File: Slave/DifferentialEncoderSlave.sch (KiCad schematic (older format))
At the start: 18 parts, among them J1 RJ45_Shielded, U1 SN75C1167, U2 MA730, U3 LDFM33PVR

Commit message: Minor change to encoder transceiver
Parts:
- U1: symbol Wetmelon:SN75C1167 -> DifferentialEncoderSlave-rescue:SN75C1167-Wetmelon
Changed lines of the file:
@@
 $EndDescr
 $Comp
-L Wetmelon:SN75C1167 U1
+L DifferentialEncoderSlave-rescue:SN75C1167-Wetmelon U1
 U 1 1 5F8ED6E6
 P 5750 2650

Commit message: Update Slave
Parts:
- removed C?: 10nF, symbol Device:C_Small
- C1: value 10nF -> 1uF; footprint (none) -> Capacitor_SMD:C_0805_2012Metric
- C2: value 100nF -> 4.7uF; footprint (none) -> Capacitor_SMD:C_0805_2012Metric
- C3, C4, C5, C6: renamed from C?; footprint (none) -> Capacitor_SMD:C_0603_1608Metric
- J1: footprint (none) -> Connector_RJ:RJ45_Amphenol_RJHSE5380
- R1, R2: footprint (none) -> Resistor_SMD:R_0603_1608Metric
- R3, R4, R5, R6, R7: renamed from R?; footprint (none) -> Resistor_SMD:R_0603_1608Metric
- U1: footprint (none) -> Package_SO:TSSOP-16_4.4x5mm_P0.65mm
- U2: footprint Package_DFN_QFN:QFN-16-1EP_3x3mm_P0.5mm_EP1.8x1.8mm -> Package_DFN_QFN:QFN-16-1EP_3x3mm_P0.5mm_EP1.7x1.7mm
- U3: footprint (none) -> Wetmelon:DFN6-2x2; symbol Wetmelon:LDFM33PVR -> DifferentialEncoderSlave-rescue:LDFM33PVR-Wetmelon
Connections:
- wire segments 80 -> 78
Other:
- note added: "Placed close to both\nLDO and MA702"

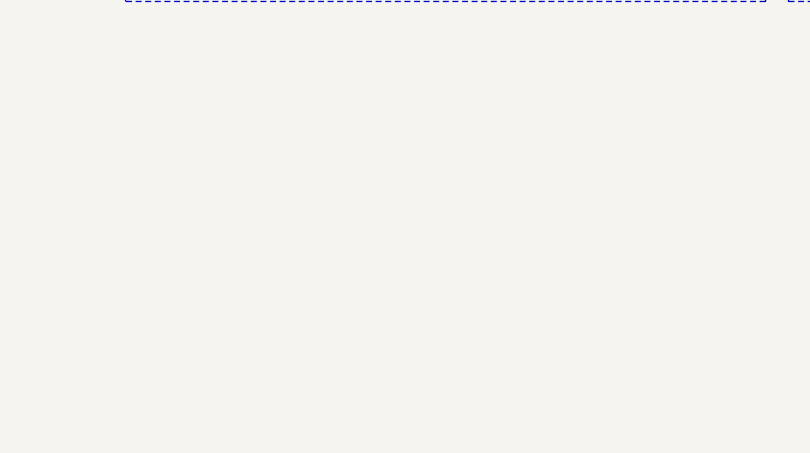
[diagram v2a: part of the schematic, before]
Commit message: Update board outline
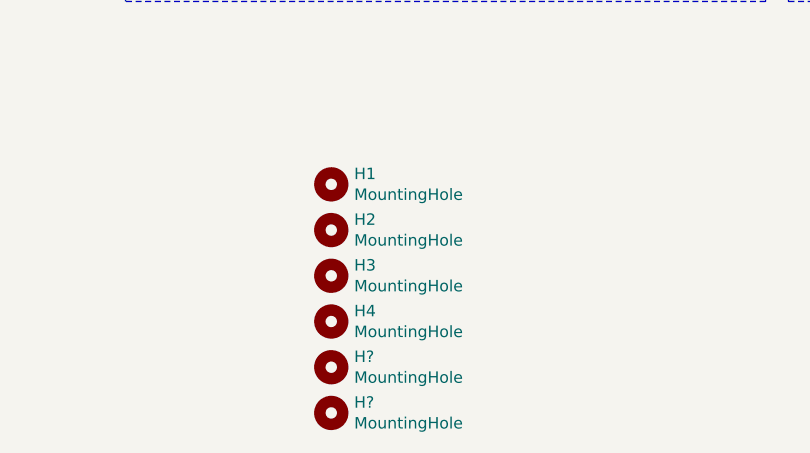
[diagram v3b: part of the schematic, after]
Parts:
- added H1, H2, H3, H4, H? (x2): MountingHole, MountingHole:MountingHole_3.2mm_M3_DIN965, symbol Mechanical:MountingHole
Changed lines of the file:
@@
+	1    0    0    -1
+$EndComp
+$Comp
+L Mechanical:MountingHole H1
+U 1 1 5FCC53CC
+P 5450 6550
+F 0 "H1" H 5550 6596 50  0000 L CNN
+F 1 "MountingHole" H 5550 6505 50  0000 L CNN
+F 2 "MountingHole:MountingHole_3.2mm_M3_DIN965" H 5450 6550 50  0001 C CNN
+F 3 "~" H 5450 6550 50  0001 C CNN
+	1    5450 6550
+	1    0    0    -1
+$EndComp
+$Comp
+L Mechanical:MountingHole H2
+U 1 1 5FCC63AC
+P 5450 6750
+F 0 "H2" H 5550 6796 50  0000 L CNN
+F 1 "MountingHole" H 5550 6705 50  0000 L CNN
+F 2 "MountingHole:MountingHole_3.2mm_M3_DIN965" H 5450 6750 50  0001 C CNN
+F 3 "~" H 5450 6750 50  0001 C CNN
+	1    5450 6750
+	1    0    0    -1
+$EndComp
+$Comp
+L Mechanical:MountingHole H3
+U 1 1 5FCC6701
+P 5450 6950
+F 0 "H3" H 5550 6996 50  0000 L CNN
+F 1 "MountingHole" H 5550 6905 50  0000 L CNN
+F 2 "MountingHole:MountingHole_3.2mm_M3_DIN965" H 5450 6950 50  0001 C CNN
+F 3 "~" H 5450 6950 50  0001 C CNN
+	1    5450 6950
+	1    0    0    -1
+$EndComp
+$Comp
+L Mechanical:MountingHole H4
+U 1 1 5FCC692E
+P 5450 7150
+F 0 "H4" H 5550 7196 50  0000 L CNN
+F 1 "MountingHole" H 5550 7105 50  0000 L CNN
+F 2 "MountingHole:MountingHole_3.2mm_M3_DIN965" H 5450 7150 50  0001 C CNN
+F 3 "~" H 5450 7150 50  0001 C CNN
+	1    5450 7150
+	1    0    0    -1
+$EndComp
+$Comp
+L Mechanical:MountingHole H?
+U 1 1 5FCE01C3
+P 5450 7350
+F 0 "H?" H 5550 7396 50  0000 L CNN
+F 1 "MountingHole" H 5550 7305 50  0000 L CNN
+F 2 "MountingHole:MountingHole_3.2mm_M3_DIN965" H 5450 7350 50  0001 C CNN
+F 3 "~" H 5450 7350 50  0001 C CNN
+	1    5450 7350
+	1    0    0    -1
+$EndComp
+$Comp
+L Mechanical:MountingHole H?
+U 1 1 5FCE01C9
+P 5450 7550
+F 0 "H?" H 5550 7596 50  0000 L CNN
+F 1 "MountingHole" H 5550 7505 50  0000 L CNN
+F 2 "MountingHole:MountingHole_3.2mm_M3_DIN965" H 5450 7550 50  0001 C CNN
+F 3 "~" H 5450 7550 50  0001 C CNN
+	1    5450 7550
 	1    0    0    -1
 $EndComp

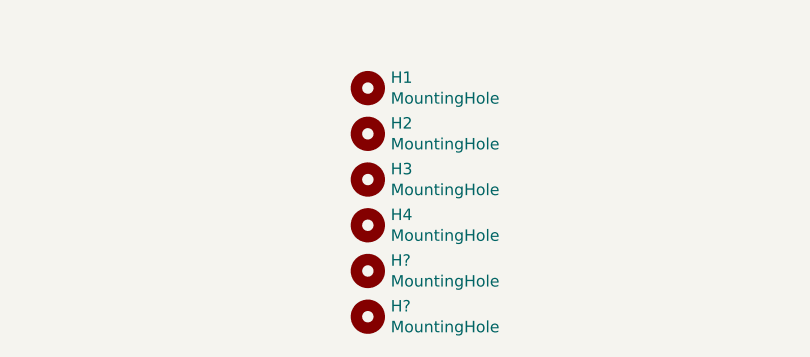
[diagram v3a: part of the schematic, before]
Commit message: Use 3mm holes
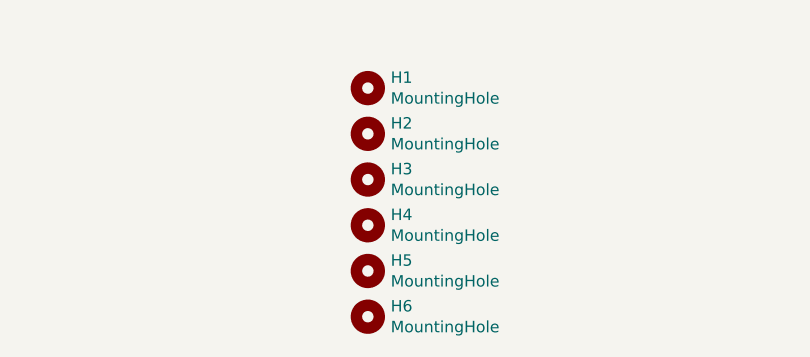
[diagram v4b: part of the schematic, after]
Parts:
- H1, H2, H3, H4: footprint MountingHole:MountingHole_3.2mm_M3_DIN965 -> MountingHole:MountingHole_3mm
- H5, H6: renamed from H?; footprint MountingHole:MountingHole_3.2mm_M3_DIN965 -> MountingHole:MountingHole_3mm
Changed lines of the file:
@@
 F 0 "H1" H 5550 6596 50  0000 L CNN
 F 1 "MountingHole" H 5550 6505 50  0000 L CNN
-F 2 "MountingHole:MountingHole_3.2mm_M3_DIN965" H 5450 6550 50  0001 C CNN
+F 2 "MountingHole:MountingHole_3mm" H 5450 6550 50  0001 C CNN
 F 3 "~" H 5450 6550 50  0001 C CNN
 	1    5450 6550
@@
 F 0 "H2" H 5550 6796 50  0000 L CNN
 F 1 "MountingHole" H 5550 6705 50  0000 L CNN
-F 2 "MountingHole:MountingHole_3.2mm_M3_DIN965" H 5450 6750 50  0001 C CNN
+F 2 "MountingHole:MountingHole_3mm" H 5450 6750 50  0001 C CNN
 F 3 "~" H 5450 6750 50  0001 C CNN
 	1    5450 6750
@@
 F 0 "H3" H 5550 6996 50  0000 L CNN
 F 1 "MountingHole" H 5550 6905 50  0000 L CNN
-F 2 "MountingHole:MountingHole_3.2mm_M3_DIN965" H 5450 6950 50  0001 C CNN
+F 2 "MountingHole:MountingHole_3mm" H 5450 6950 50  0001 C CNN
 F 3 "~" H 5450 6950 50  0001 C CNN
 	1    5450 6950
@@
 F 0 "H4" H 5550 7196 50  0000 L CNN
 F 1 "MountingHole" H 5550 7105 50  0000 L CNN
-F 2 "MountingHole:MountingHole_3.2mm_M3_DIN965" H 5450 7150 50  0001 C CNN
+F 2 "MountingHole:MountingHole_3mm" H 5450 7150 50  0001 C CNN
 F 3 "~" H 5450 7150 50  0001 C CNN
 	1    5450 7150
@@
 $EndComp
 $Comp
-L Mechanical:MountingHole H?
+L Mechanical:MountingHole H5
 U 1 1 5FCE01C3
 P 5450 7350
-F 0 "H?" H 5550 7396 50  0000 L CNN
+F 0 "H5" H 5550 7396 50  0000 L CNN
 F 1 "MountingHole" H 5550 7305 50  0000 L CNN
-F 2 "MountingHole:MountingHole_3.2mm_M3_DIN965" H 5450 7350 50  0001 C CNN
+F 2 "MountingHole:MountingHole_3mm" H 5450 7350 50  0001 C CNN
 F 3 "~" H 5450 7350 50  0001 C CNN
 	1    5450 7350
@@
 $EndComp
 $Comp
-L Mechanical:MountingHole H?
+L Mechanical:MountingHole H6
 U 1 1 5FCE01C9
 P 5450 7550
-F 0 "H?" H 5550 7596 50  0000 L CNN
+F 0 "H6" H 5550 7596 50  0000 L CNN
 F 1 "MountingHole" H 5550 7505 50  0000 L CNN
-F 2 "MountingHole:MountingHole_3.2mm_M3_DIN965" H 5450 7550 50  0001 C CNN
+F 2 "MountingHole:MountingHole_3mm" H 5450 7550 50  0001 C CNN
 F 3 "~" H 5450 7550 50  0001 C CNN
 	1    5450 7550

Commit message: Update Slave with circular keepout, SMD RJ 45
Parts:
- J1: footprint Connector_RJ:RJ45_Amphenol_RJHSE5380 -> Wetmelon:RJLSE4118101
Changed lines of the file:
@@
 F 0 "J1" H 8320 2839 50  0000 R CNN
 F 1 "RJ45_Shielded" H 8320 2748 50  0000 R CNN
-F 2 "Connector_RJ:RJ45_Amphenol_RJHSE5380" V 8650 2825 50  0001 C CNN
+F 2 "Wetmelon:RJLSE4118101" V 8650 2825 50  0001 C CNN
 F 3 "~" V 8650 2825 50  0001 C CNN
 	1    8650 2800

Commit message: Export master BOM
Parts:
- H5, H6: footprint MountingHole:MountingHole_3mm -> MountingHole:MountingHole_3.2mm_M3_DIN965
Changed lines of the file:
@@
 F 0 "H5" H 5550 7396 50  0000 L CNN
 F 1 "MountingHole" H 5550 7305 50  0000 L CNN
-F 2 "MountingHole:MountingHole_3mm" H 5450 7350 50  0001 C CNN
+F 2 "MountingHole:MountingHole_3.2mm_M3_DIN965" H 5450 7350 50  0001 C CNN
 F 3 "~" H 5450 7350 50  0001 C CNN
 	1    5450 7350
@@
 F 0 "H6" H 5550 7596 50  0000 L CNN
 F 1 "MountingHole" H 5550 7505 50  0000 L CNN
-F 2 "MountingHole:MountingHole_3mm" H 5450 7550 50  0001 C CNN
+F 2 "MountingHole:MountingHole_3.2mm_M3_DIN965" H 5450 7550 50  0001 C CNN
 F 3 "~" H 5450 7550 50  0001 C CNN
 	1    5450 7550

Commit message: Encoder side TSSOP -> SOP 5.3x6.2
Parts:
- U1: footprint Package_SO:TSSOP-16_4.4x5mm_P0.65mm -> Package_SO:SSOP-16_5.3x6.2mm_P0.65mm
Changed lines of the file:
@@
 F 0 "U1" H 5250 3650 50  0000 C CNN
 F 1 "SN75C1167" H 5400 3550 50  0000 C CNN
-F 2 "Package_SO:TSSOP-16_4.4x5mm_P0.65mm" H 5750 3550 50  0001 C CNN
+F 2 "Package_SO:SSOP-16_5.3x6.2mm_P0.65mm" H 5750 3550 50  0001 C CNN
 F 3 "" H 5750 3550 50  0001 C CNN
 	1    5750 2650

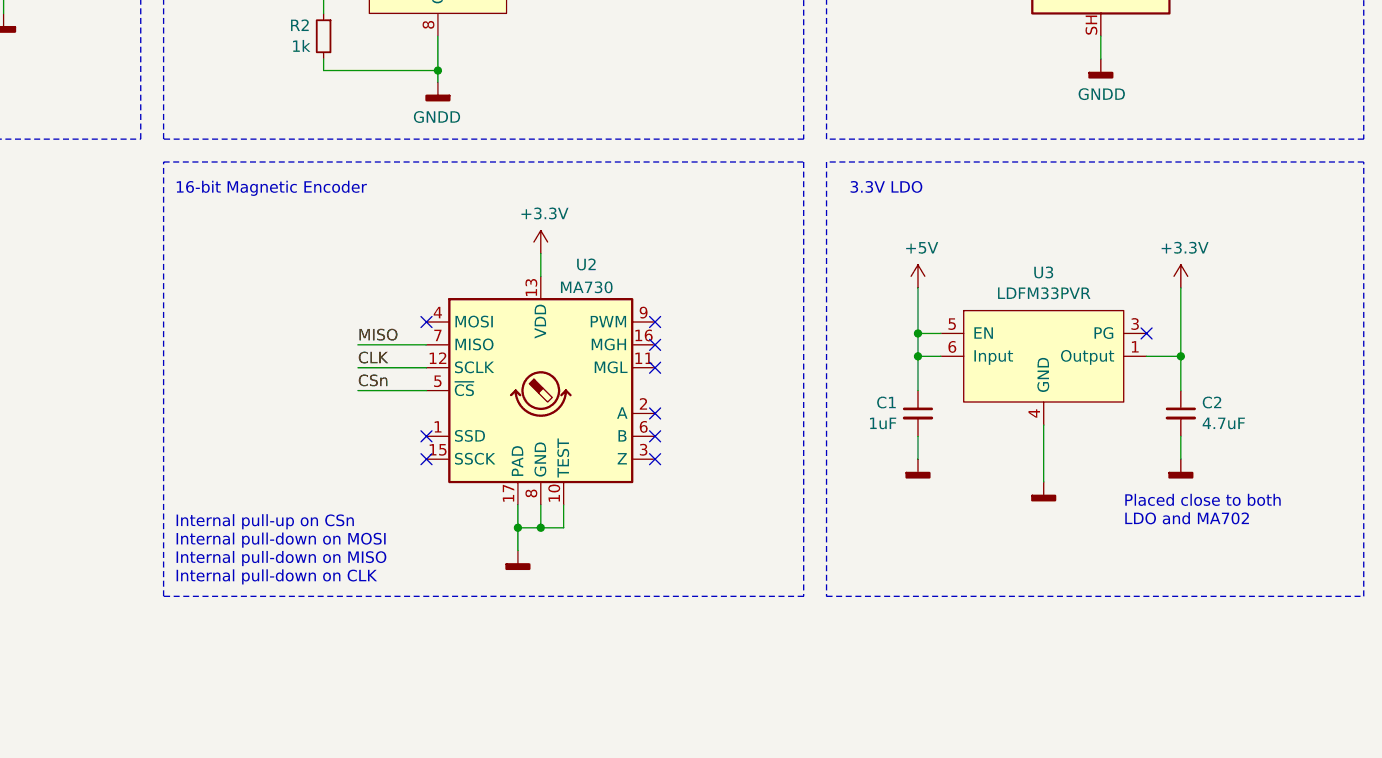
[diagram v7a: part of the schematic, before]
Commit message: Create AEAT-9922 encoder variant
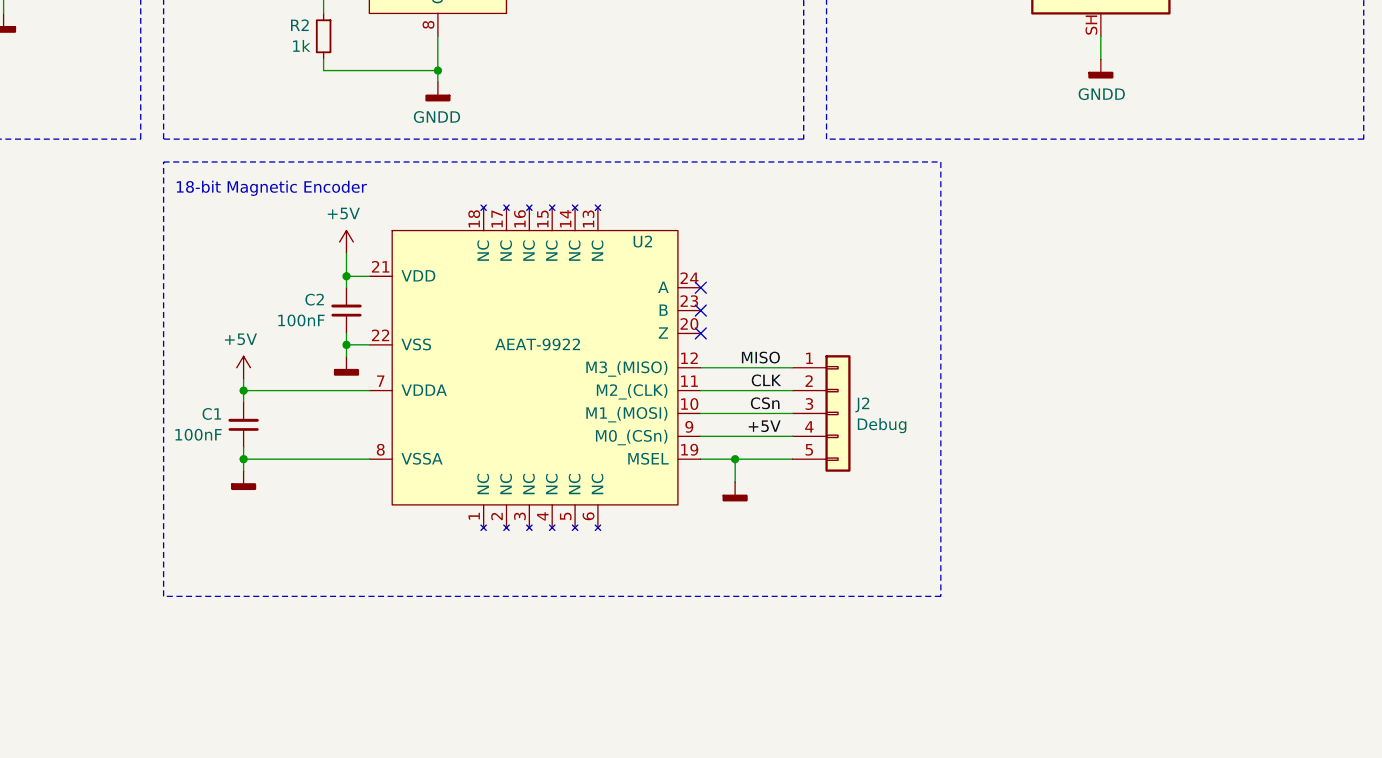
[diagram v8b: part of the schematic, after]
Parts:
- removed U2: MA730, Package_DFN_QFN:QFN-16-1EP_3x3mm_P0.5mm_EP1.7x1.7mm, symbol Sensor_Magnetic:MA730
- removed U3: LDFM33PVR, Wetmelon:DFN6-2x2, symbol DifferentialEncoderSlave-rescue:LDFM33PVR-Wetmelon
- added J2: Debug, Connector_PinHeader_2.54mm:PinHeader_1x05_P2.54mm_Vertical, symbol Connector_Generic:Conn_01x05
- added U2: AEAT-9922, Package_DFN_QFN:QFN-24-1EP_4x4mm_P0.5mm_EP2.7x2.7mm, symbol Wetmelon:AEAT-9922
- C1: value 1uF -> 100nF; footprint Capacitor_SMD:C_0805_2012Metric -> Capacitor_SMD:C_0603_1608Metric
- C2: value 4.7uF -> 100nF; footprint Capacitor_SMD:C_0805_2012Metric -> Capacitor_SMD:C_0603_1608Metric
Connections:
- net +3V3 is gone; now on net GNDD: C2.1
- net +5V: now also C1.2, C2.2, J2.4 (Pin_4), U2.21 (VDD), U2.7 (VDDA), U2.9 (M0_(CSn)); no longer C1.1
- net CLK: now also J2.2 (Pin_2), U2.11 (M2_(CLK))
- net CSn: now also J2.3 (Pin_3), U2.10 (M1_(MOSI))
- net GNDD: now also C1.1, J2.5 (Pin_5), U2.19 (MSEL), U2.22 (VSS), U2.25 (VSS), U2.8 (VSSA); no longer C1.2, C2.2
- net MISO: now also J2.1 (Pin_1), U2.12 (M3_(MISO))
- no-connect marks 13 -> 6
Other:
- note added: "18-bit Magnetic Encoder"
- note removed: "16-bit Magnetic Encoder"
- note removed: "3.3V LDO"
- note removed: "Internal pull-up on CSn\nInternal pull-down on MOSI\nInternal pull-down on MISO\nInternal pull-down on CLK"
- note removed: "Placed close to both\nLDO and MA702"
